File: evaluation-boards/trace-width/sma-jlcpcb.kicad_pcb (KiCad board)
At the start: 4 copper layers, 80 x 60 mm, 12 parts, among them J11 CONN_COAXIAL, J12 CONN_COAXIAL

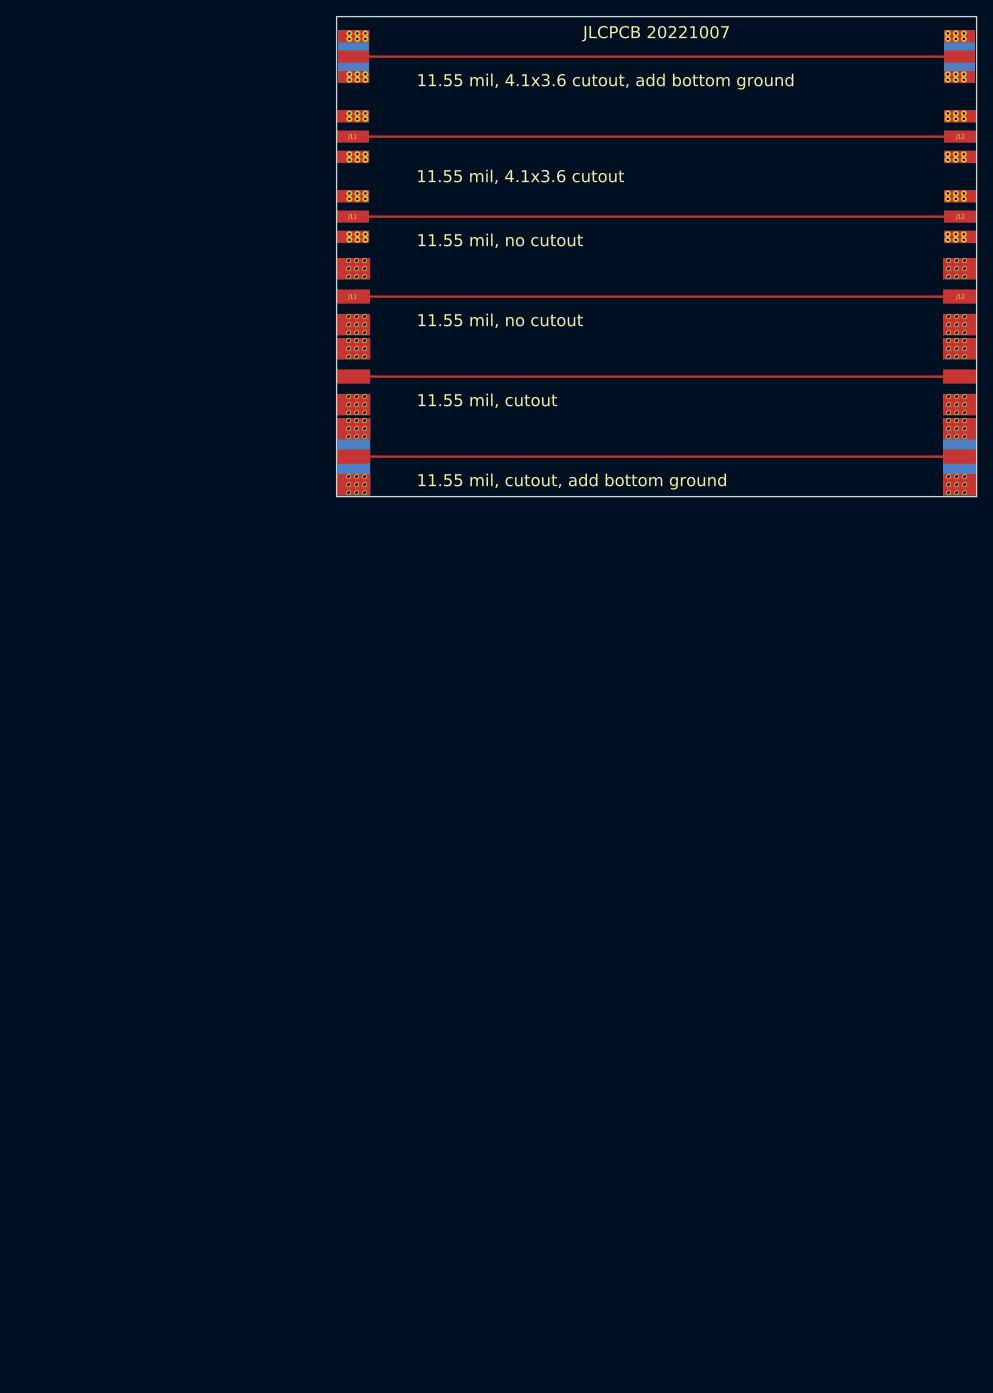
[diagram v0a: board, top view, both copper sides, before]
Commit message: Update trace width and SMA connector boards
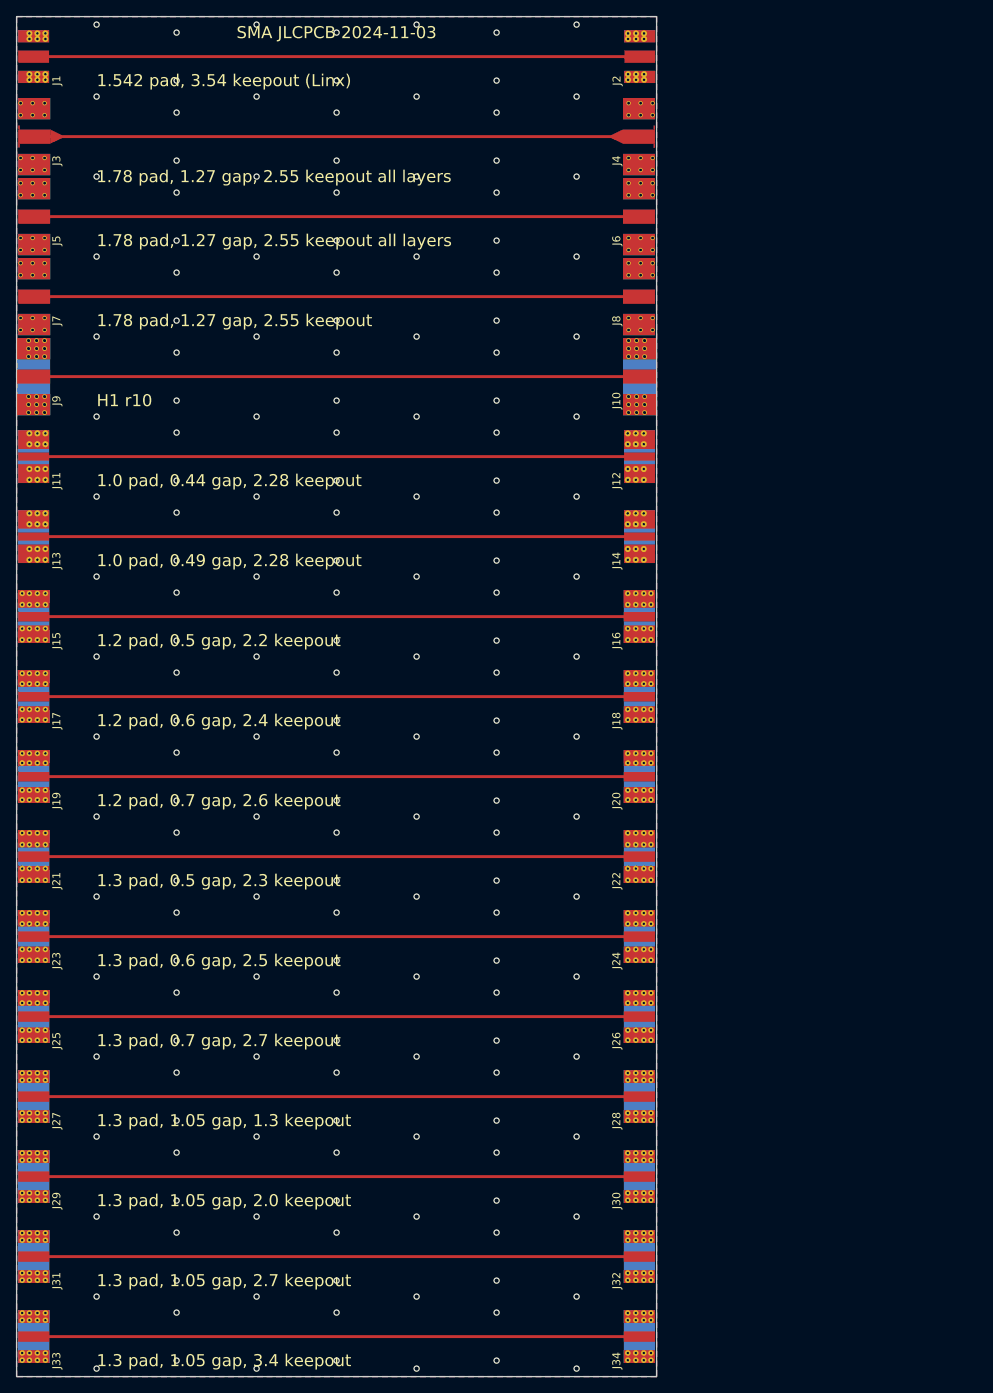
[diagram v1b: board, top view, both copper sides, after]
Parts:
- removed the J11 at (120.0, 60.0)
- removed the J11 at (120.0, 20.0)
- removed the J12 at (200.0, 60.0)
- removed the J12 at (200.0, 20.0)
- added J1: Conn_Coaxial, sma-variants:Linx_SMA_CONSMA003.062, F.Cu at (80.0, 20.0)
- added J11: Conn_Coaxial, sma-variants:SMA-EDGE-1mm-pad-0.44mm-gap, F.Cu at (80.0, 70.0)
- added J12: Conn_Coaxial, sma-variants:SMA-EDGE-1mm-pad-0.44mm-gap, F.Cu at (160.0, 70.0)
- added J13: Conn_Coaxial, sma-variants:SMA-EDGE-1mm-pad-0.49mm-gap, F.Cu at (80.0, 80.0)
- added J14: Conn_Coaxial, sma-variants:SMA-EDGE-1mm-pad-0.49mm-gap, F.Cu at (160.0, 80.0)
- added J15: Conn_Coaxial, sma-variants:SMA-EDGE-1.2mm-pad-0.5mm-gap-2.2mm-keepout, F.Cu at (80.0, 90.0)
- added J16: Conn_Coaxial, sma-variants:SMA-EDGE-1.2mm-pad-0.5mm-gap-2.2mm-keepout, F.Cu at (160.0, 90.0)
- added J17: Conn_Coaxial, sma-variants:SMA-EDGE-1.2mm-pad-0.6mm-gap-2.4mm-keepout, F.Cu at (80.0, 100.0)
- added J18: Conn_Coaxial, sma-variants:SMA-EDGE-1.2mm-pad-0.6mm-gap-2.4mm-keepout, F.Cu at (160.0, 100.0)
- added J19: Conn_Coaxial, sma-variants:SMA-EDGE-1.2mm-pad-0.7mm-gap-2.6mm-keepout, F.Cu at (80.0, 110.0)
- added J2: Conn_Coaxial, sma-variants:Linx_SMA_CONSMA003.062, F.Cu at (160.0, 20.0)
- added J20: Conn_Coaxial, sma-variants:SMA-EDGE-1.2mm-pad-0.7mm-gap-2.6mm-keepout, F.Cu at (160.0, 110.0)
- added J21: Conn_Coaxial, sma-variants:SMA-EDGE-1.3mm-pad-0.5mm-gap-2.3mm-keepout, F.Cu at (80.0, 120.0)
- added J22: Conn_Coaxial, sma-variants:SMA-EDGE-1.3mm-pad-0.5mm-gap-2.3mm-keepout, F.Cu at (160.0, 120.0)
- added J23: Conn_Coaxial, sma-variants:SMA-EDGE-1.3mm-pad-0.6mm-gap-2.5mm-keepout, F.Cu at (80.0, 130.0)
- added J24: Conn_Coaxial, sma-variants:SMA-EDGE-1.3mm-pad-0.6mm-gap-2.5mm-keepout, F.Cu at (160.0, 130.0)
- added J25: Conn_Coaxial, sma-variants:SMA-EDGE-1.3mm-pad-0.7mm-gap-2.7mm-keepout, F.Cu at (80.0, 140.0)
- added J26: Conn_Coaxial, sma-variants:SMA-EDGE-1.3mm-pad-0.7mm-gap-2.7mm-keepout, F.Cu at (160.0, 140.0)
- added J27: Conn_Coaxial, sma-variants:SMA-EDGE-1.3mm-pad-1.05mm-gap-1.3mm-keepout, F.Cu at (80.0, 150.0)
- added J28: Conn_Coaxial, sma-variants:SMA-EDGE-1.3mm-pad-1.05mm-gap-1.3mm-keepout, F.Cu at (160.0, 150.0)
- added J29: Conn_Coaxial, sma-variants:SMA-EDGE-1.3mm-pad-1.05mm-gap-2.0mm-keepout, F.Cu at (80.0, 160.0)
- added J30: Conn_Coaxial, sma-variants:SMA-EDGE-1.3mm-pad-1.05mm-gap-2.0mm-keepout, F.Cu at (160.0, 160.0)
- added J31: Conn_Coaxial, sma-variants:SMA-EDGE-1.3mm-pad-1.05mm-gap-2.7mm-keepout, F.Cu at (80.0, 170.0)
- added J32: Conn_Coaxial, sma-variants:SMA-EDGE-1.3mm-pad-1.05mm-gap-2.7mm-keepout, F.Cu at (160.0, 170.0)
- added J33: Conn_Coaxial, sma-variants:SMA-EDGE-1.3mm-pad-1.05mm-gap-3.4mm-keepout, F.Cu at (80.0, 180.0)
- added J34: Conn_Coaxial, sma-variants:SMA-EDGE-1.3mm-pad-1.05mm-gap-3.4mm-keepout, F.Cu at (160.0, 180.0)
- J10: renamed from J12; value CONN_COAXIAL -> Conn_Coaxial
- J3: renamed from J11; value CONN_COAXIAL -> Conn_Coaxial; footprint gsg-modules:SMA-EDGE -> sma-variants:SMA_EdgeMount_Horizontal
- J4: renamed from J12; value CONN_COAXIAL -> Conn_Coaxial; footprint gsg-modules:SMA-EDGE -> sma-variants:SMA_EdgeMount_Horizontal
- J5: renamed from J11; value CONN_COAXIAL -> Conn_Coaxial; footprint gsg-modules:SMA-EDGE -> sma-variants:SMA_EdgeMount_Horizontal_Simplified
- J6: renamed from J12; value CONN_COAXIAL -> Conn_Coaxial; footprint gsg-modules:SMA-EDGE -> sma-variants:SMA_EdgeMount_Horizontal_Simplified
- J7: renamed from J11; value CONN_COAXIAL -> Conn_Coaxial; footprint gsg-modules:SMA-73251-2120 -> sma-variants:SMA_EdgeMount_Horizontal_Simplified
- J8: renamed from J12; value CONN_COAXIAL -> Conn_Coaxial; footprint gsg-modules:SMA-73251-2120 -> sma-variants:SMA_EdgeMount_Horizontal_Simplified
- J9: renamed from J11; value CONN_COAXIAL -> Conn_Coaxial
- moved J10 41.2 mm to (160.0, 60.0)
- moved J9 41.2 mm to (80.0, 60.0)
- moved J3 40.0 mm to (80.0, 30.0), turned to 180 degrees
- moved J4 40.0 mm to (160.0, 30.0), turned to 0 degrees
- moved J5 40.0 mm to (80.0, 40.0), turned to 180 degrees
- moved J6 40.0 mm to (160.0, 40.0), turned to 0 degrees
- moved J7 40.0 mm to (80.0, 50.0), turned to 180 degrees
- moved J8 40.0 mm to (160.0, 50.0), turned to 0 degrees
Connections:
- J10 pad 1: Net-(J11-Pad1) -> Net-(J10-In)
- J3 pad 1: Net-(J11-Pad1) -> Net-(J3-In)
- J4 pad 1: Net-(J11-Pad1) -> Net-(J3-In)
- J5 pad 1: Net-(J11-Pad1) -> Net-(J5-In)
- J6 pad 1: Net-(J11-Pad1) -> Net-(J5-In)
- J7 pad 1: Net-(J11-Pad1) -> Net-(J7-In)
- J8 pad 1: Net-(J11-Pad1) -> Net-(J7-In)
- J9 pad 1: Net-(J11-Pad1) -> Net-(J10-In)
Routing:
- net Net-(J11-Pad1): track 454.9 -> 0.00 mm
- net Net-(J7-In): track 0.00 -> 75.8 mm
- net Net-(J5-In): track 0.00 -> 75.8 mm
- net Net-(J3-In): track 0.00 -> 75.8 mm
- net Net-(J11-In): track 0.00 -> 75.8 mm
- net Net-(J10-In): track 0.00 -> 75.8 mm
- net Net-(J1-In): track 0.00 -> 75.8 mm
- net Net-(J13-In): track 0.00 -> 75.7 mm
- net Net-(J33-In): track 0.00 -> 75.7 mm
- net Net-(J31-In): track 0.00 -> 75.7 mm
- net Net-(J29-In): track 0.00 -> 75.7 mm
- net Net-(J27-In): track 0.00 -> 75.7 mm
- net Net-(J25-In): track 0.00 -> 75.7 mm
- net Net-(J23-In): track 0.00 -> 75.7 mm
- net Net-(J21-In): track 0.00 -> 75.7 mm
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- added copper zone on B.Cu, net GND
- added copper zone on F.Cu, net GND
- added copper zone on In2.Cu, net GND
- added copper zone on In3.Cu, net GND
- added copper zone on In4.Cu, net GND
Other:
- board size 80 x 60 mm -> 80 x 170 mm
- copper layers 4 -> 6
- board text added: "1.0 pad, 0.44 gap, 2.28 keepout"
- board text added: "1.0 pad, 0.49 gap, 2.28 keepout"
- board text added: "1.2 pad, 0.5 gap, 2.2 keepout"
- board text added: "1.2 pad, 0.6 gap, 2.4 keepout"
- board text added: "1.2 pad, 0.7 gap, 2.6 keepout"
- board text added: "1.3 pad, 0.5 gap, 2.3 keepout"
- board text added: "1.3 pad, 0.6 gap, 2.5 keepout"
- board text added: "1.3 pad, 0.7 gap, 2.7 keepout"
- board text added: "1.3 pad, 1.05 gap, 1.3 keepout"
- board text added: "1.3 pad, 1.05 gap, 2.0 keepout"
- board text added: "1.3 pad, 1.05 gap, 2.7 keepout"
- board text added: "1.3 pad, 1.05 gap, 3.4 keepout"
- board text added: "1.542 pad, 3.54 keepout (Linx)"
- board text added: "1.78 pad, 1.27 gap, 2.55 keepout"
- board text added: "1.78 pad, 1.27 gap, 2.55 keepout all layers"
- board text added: "H1 r10"
- board text added: "SMA JLCPCB 2024-11-03"
- board text removed: "11.55 mil, 4.1x3.6 cutout"
- board text removed: "11.55 mil, 4.1x3.6 cutout, add bottom ground"
- board text removed: "11.55 mil, cutout"
- board text removed: "11.55 mil, cutout, add bottom ground"
- board text removed: "11.55 mil, no cutout"
- board text removed: "JLCPCB 20221007"

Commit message: Update SMA connector board
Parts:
- removed J21, J22: Conn_Coaxial, sma-variants:SMA-EDGE-1.3mm-pad-0.5mm-gap-2.3mm-keepout
- removed J23, J24: Conn_Coaxial, sma-variants:SMA-EDGE-1.3mm-pad-0.6mm-gap-2.5mm-keepout
- removed J25, J26: Conn_Coaxial, sma-variants:SMA-EDGE-1.3mm-pad-0.7mm-gap-2.7mm-keepout
- removed J27, J28: Conn_Coaxial, sma-variants:SMA-EDGE-1.3mm-pad-1.05mm-gap-1.3mm-keepout
- removed J29, J30: Conn_Coaxial, sma-variants:SMA-EDGE-1.3mm-pad-1.05mm-gap-2.0mm-keepout
- removed J31, J32: Conn_Coaxial, sma-variants:SMA-EDGE-1.3mm-pad-1.05mm-gap-2.7mm-keepout
- removed J33, J34: Conn_Coaxial, sma-variants:SMA-EDGE-1.3mm-pad-1.05mm-gap-3.4mm-keepout
- J1, J2: footprint sma-variants:Linx_SMA_CONSMA003.062 -> sma-variants:SMA-EDGE-1.3mm-pad-1.05mm-gap-2.0mm-keepout
- J10, J9: footprint sma-variants:SMA-73251-2120-bgnd -> sma-variants:SMA-EDGE-1.3mm-pad-1.05mm-gap-2.4mm-keepout
- J11, J12: footprint sma-variants:SMA-EDGE-1mm-pad-0.44mm-gap -> sma-variants:SMA-EDGE-1.3mm-pad-1.05mm-gap-2.5mm-keepout
- J13, J14: footprint sma-variants:SMA-EDGE-1mm-pad-0.49mm-gap -> sma-variants:SMA-EDGE-1.3mm-pad-1.05mm-gap-2.6mm-keepout
- J15, J16: footprint sma-variants:SMA-EDGE-1.2mm-pad-0.5mm-gap-2.2mm-keepout -> sma-variants:SMA-EDGE-1.3mm-pad-1.05mm-gap-2.7mm-keepout
- J17, J18: footprint sma-variants:SMA-EDGE-1.2mm-pad-0.6mm-gap-2.4mm-keepout -> sma-variants:SMA-EDGE-1.3mm-pad-1.05mm-gap-2.8mm-keepout
- J19, J20: footprint sma-variants:SMA-EDGE-1.2mm-pad-0.7mm-gap-2.6mm-keepout -> sma-variants:SMA-EDGE-1.3mm-pad-1.05mm-gap-2.9mm-keepout
- J3, J4: footprint sma-variants:SMA_EdgeMount_Horizontal -> sma-variants:SMA-EDGE-1.3mm-pad-1.05mm-gap-2.1mm-keepout
- J5, J6: footprint sma-variants:SMA_EdgeMount_Horizontal_Simplified -> sma-variants:SMA-EDGE-1.3mm-pad-1.05mm-gap-2.2mm-keepout
- J7, J8: footprint sma-variants:SMA_EdgeMount_Horizontal_Simplified -> sma-variants:SMA-EDGE-1.3mm-pad-1.05mm-gap-2.3mm-keepout
- turned J3 to 0 degrees
- turned J4 to 180 degrees
- turned J5 to 0 degrees
- turned J6 to 180 degrees
- turned J7 to 0 degrees
- turned J8 to 180 degrees
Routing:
- net Net-(J33-In): track 75.7 -> 0.00 mm
- net Net-(J31-In): track 75.7 -> 0.00 mm
- net Net-(J29-In): track 75.7 -> 0.00 mm
- net Net-(J27-In): track 75.7 -> 0.00 mm
- net Net-(J25-In): track 75.7 -> 0.00 mm
- net Net-(J23-In): track 75.7 -> 0.00 mm
- net Net-(J21-In): track 75.7 -> 0.00 mm
- net GND: vias 174 -> 104
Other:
- board size 80 x 170 mm -> 80 x 100 mm
- board text added: "1.3 pad, 1.05 gap, 2.1 keepout"
- board text added: "1.3 pad, 1.05 gap, 2.2 keepout"
- board text added: "1.3 pad, 1.05 gap, 2.3 keepout"
- board text added: "1.3 pad, 1.05 gap, 2.4 keepout"
- board text added: "1.3 pad, 1.05 gap, 2.5 keepout"
- board text added: "1.3 pad, 1.05 gap, 2.6 keepout"
- board text added: "1.3 pad, 1.05 gap, 2.8 keepout"
- board text added: "1.3 pad, 1.05 gap, 2.9 keepout"
- board text added: "SMA JLCPCB 2024-12-06"
- board text removed: "1.0 pad, 0.44 gap, 2.28 keepout"
- board text removed: "1.0 pad, 0.49 gap, 2.28 keepout"
- board text removed: "1.2 pad, 0.5 gap, 2.2 keepout"
- board text removed: "1.2 pad, 0.6 gap, 2.4 keepout"
- board text removed: "1.2 pad, 0.7 gap, 2.6 keepout"
- board text removed: "1.3 pad, 0.5 gap, 2.3 keepout"
- board text removed: "1.3 pad, 0.6 gap, 2.5 keepout"
- board text removed: "1.3 pad, 0.7 gap, 2.7 keepout"
- board text removed: "1.3 pad, 1.05 gap, 1.3 keepout"
- board text removed: "1.3 pad, 1.05 gap, 3.4 keepout"
- board text removed: "1.542 pad, 3.54 keepout (Linx)"
- board text removed: "1.78 pad, 1.27 gap, 2.55 keepout"
- board text removed: "1.78 pad, 1.27 gap, 2.55 keepout all layers"
- board text removed: "H1 r10"
- board text removed: "SMA JLCPCB 2024-11-03"

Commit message: Update SMA connector board
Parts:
- J1, J2: footprint sma-variants:SMA-EDGE-1.3mm-pad-1.05mm-gap-2.0mm-keepout -> sma-variants:SMA-EDGE-1.6mm-pad-1.1mm-gap-2.2mm-keepout
- J10, J9: footprint sma-variants:SMA-EDGE-1.3mm-pad-1.05mm-gap-2.4mm-keepout -> sma-variants:SMA-EDGE-1.6mm-pad-1.1mm-gap-3.8mm-keepout
- J3, J4: footprint sma-variants:SMA-EDGE-1.3mm-pad-1.05mm-gap-2.1mm-keepout -> sma-variants:SMA-EDGE-1.6mm-pad-1.1mm-gap-2.6mm-keepout
- J5, J6: footprint sma-variants:SMA-EDGE-1.3mm-pad-1.05mm-gap-2.2mm-keepout -> sma-variants:SMA-EDGE-1.6mm-pad-1.1mm-gap-3.0mm-keepout
- J7, J8: footprint sma-variants:SMA-EDGE-1.3mm-pad-1.05mm-gap-2.3mm-keepout -> sma-variants:SMA-EDGE-1.6mm-pad-1.1mm-gap-3.4mm-keepout
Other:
- board text added: "1.6 pad, 1.1 gap, 2.2 keepout"
- board text added: "1.6 pad, 1.1 gap, 2.6 keepout"
- board text added: "1.6 pad, 1.1 gap, 3.0 keepout"
- board text added: "1.6 pad, 1.1 gap, 3.4 keepout"
- board text added: "1.6 pad, 1.1 gap, 3.8 keepout"
- board text added: "SMA JLCPCB 2025-03-11"
- board text removed: "1.3 pad, 1.05 gap, 2.0 keepout"
- board text removed: "1.3 pad, 1.05 gap, 2.1 keepout"
- board text removed: "1.3 pad, 1.05 gap, 2.2 keepout"
- board text removed: "1.3 pad, 1.05 gap, 2.3 keepout"
- board text removed: "1.3 pad, 1.05 gap, 2.4 keepout"
- board text removed: "SMA JLCPCB 2024-12-06"
